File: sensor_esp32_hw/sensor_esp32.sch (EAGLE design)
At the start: 31 parts, among them IC1 ESP32-C3-WROOM-02-N4, IC2 ESP32-WROOM-32UE-N16, Q1 DMG3415, U1 AHT20, U2 TPL5110

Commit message: minor improvements before fabrication
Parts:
- added C10, C11: 100 nF, microbuilder:CAP_CERAMIC_0603
- C3: value 22 uF -> 10 uF
- PS1: value AP2202K-3.3TRG1 -> LDI8119-3.3EN-DIO
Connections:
- net GND: now also C10.2, C11.2
- net N$1: now also IC1.IO3; no longer IC1.IO2
- net PWROUT: now also C11.1; no longer C2.+
- net PWROUT_DIV: now also C10.1
- net VCC: now also C2.+
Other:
- moved on the sheet: C2, C3, PS1, R7

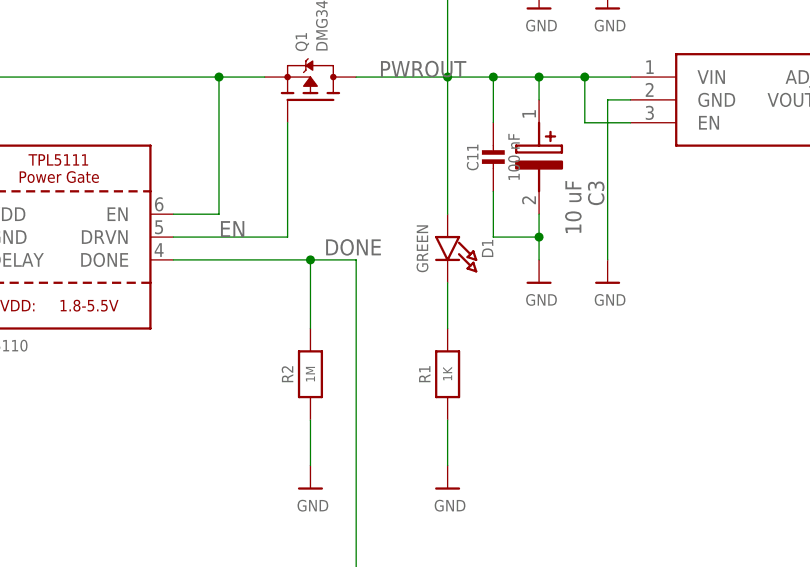
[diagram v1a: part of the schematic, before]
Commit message: fixes to schematic and pcb, also made esp32 sensor work
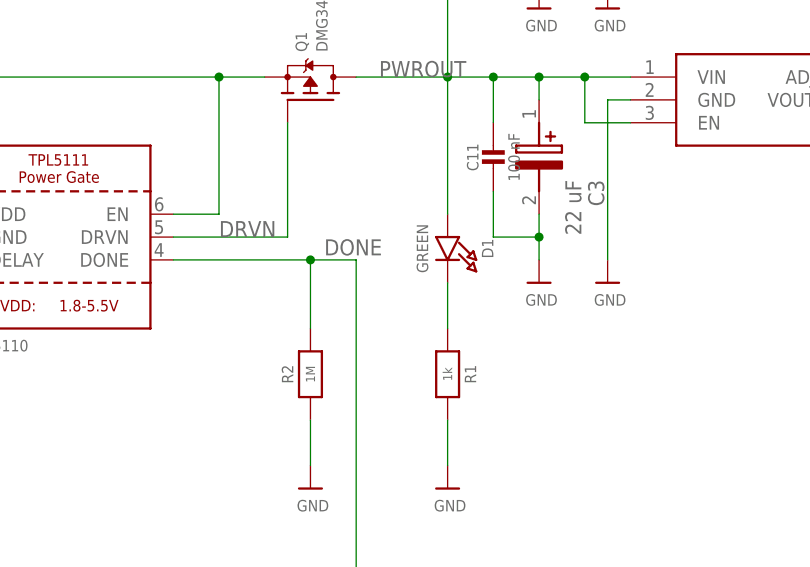
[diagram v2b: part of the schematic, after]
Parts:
- C3: value 10 uF -> 22 uF; DESCRIPTION (none) -> Solid Tantalum Surface Mount Chip Capacitors TANTAMOUNT(TM)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; HEIGHT (none) -> 1.8mm; MANUFACTURER_NAME (none) -> Vishay; MANUFACTURER_PART_NUMBER (none) -> 293D226X9010A2TE3
- C5: device microbuilder:CAP_CERAMIC0805-NOOUTLINE -> microbuilder:CAP_CERAMIC_0603
- R1: value 1K -> 1k; device microbuilder:RESISTOR0805_NOOUTLINE -> microbuilder:RESISTOR_0603
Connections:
- new net DRVN: Q1.G, U2.DRVN
- net EN: no longer Q1.G, U2.DRVN
- net GND: now also R1.2; no longer R1.1
- net N$3: now also R1.1; no longer R1.2
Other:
- moved on the sheet: R1
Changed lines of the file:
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@@
 <part name="Q1" library="microbuilder" deviceset="MOSFET-P" device="WIDE" value="DMG3415"/>
 <part name="D1" library="microbuilder" deviceset="LED" device="0805_NOOUTLINE" value="GREEN"/>
-<part name="R1" library="microbuilder" deviceset="RESISTOR" device="0805_NOOUTLINE" value="1K"/>
 <part name="U$6" library="microbuilder" deviceset="GND" device=""/>
 <part name="R2" library="microbuilder" deviceset="RESISTOR" device="_0603" value="1M"/>
@@
 <part name="JP1" library="jumper" deviceset="JP1E" device=""/>
 <part name="C2" library="293D107X9010C2TE3" deviceset="293D107X9010C2TE3" device="" value="100 uF"/>
-<part name="C3" library="293D226X9010A2TE3" deviceset="293D226X9010A2TE3" device="" value="10 uF"/>
 <part name="IC1" library="ESP32-C3-WROOM-02-N4" deviceset="ESP32-C3-WROOM-02-N4" device=""/>
 <part name="U$1" library="microbuilder" deviceset="GND" device=""/>
@@
 <part name="U$5" library="microbuilder" deviceset="GND" device=""/>
 <part name="U$8" library="microbuilder" deviceset="GND" device=""/>
-<part name="C5" library="microbuilder" deviceset="CAP_CERAMIC" device="0805-NOOUTLINE" value="100 nF"/>
 <part name="SV2" library="con-lstb" deviceset="MA03-1" device=""/>
 <part name="U$12" library="microbuilder" deviceset="GND" device=""/>
@@
 <part name="U$19" library="microbuilder" deviceset="GND" device=""/>
 <part name="C11" library="microbuilder" deviceset="CAP_CERAMIC" device="_0603" value="100 nF"/>
+<part name="C5" library="microbuilder" deviceset="CAP_CERAMIC" device="_0603" value="100 nF"/>
+<part name="R1" library="microbuilder" deviceset="RESISTOR" device="_0603" value="1k"/>
+<part name="C3" library="293D226X9010A2TE3" deviceset="293D226X9010A2TE3" device="" value="22 uF">
+<attribute name="DESCRIPTION" value="Solid Tantalum Surface Mount Chip Capacitors TANTAMOUNT(TM), Molded Case, Standard Industrial Grade"/>
+<attribute name="HEIGHT" value="1.8mm"/>
+<attribute name="MANUFACTURER_NAME" value="Vishay"/>
+<attribute name="MANUFACTURER_PART_NUMBER" value="293D226X9010A2TE3"/>
+<attribute name="TME_ELECTRONIC_COMPONENTS_PART_NUMBER" value=""/>
+<attribute name="TME_ELECTRONIC_COMPONENTS_PRICE-STOCK" value=""/>
+</part>
 </parts>
 <sheets>
@@
 <instance part="Q1" gate="G$1" x="160.02" y="109.22" rot="R90"/>
 <instance part="D1" gate="G$1" x="175.26" y="88.9" rot="R270"/>
-<instance part="R1" gate="G$1" x="175.26" y="76.2" rot="R90"/>
 <instance part="U$6" gate="G$1" x="175.26" y="63.5"/>
 <instance part="R2" gate="G$1" x="160.02" y="76.2" rot="R90"/>
@@
 <instance part="JP1" gate="A" x="83.82" y="96.52" rot="MR270"/>
 <instance part="C2" gate="G$1" x="228.6" y="104.14" rot="R270"/>
-<instance part="C3" gate="G$1" x="185.42" y="106.68" rot="R270"/>
 <instance part="IC1" gate="G$1" x="266.7" y="106.68"/>
 <instance part="U$1" gate="G$1" x="302.26" y="71.12"/>
@@
 <instance part="U$5" gate="G$1" x="193.04" y="86.36"/>
 <instance part="U$8" gate="G$1" x="236.22" y="83.82"/>
-<instance part="C5" gate="G$1" x="243.84" y="96.52"/>
 <instance part="SV2" gate="G$1" x="373.38" y="104.14" rot="R180"/>
 <instance part="U$12" gate="G$1" x="363.22" y="86.36"/>
@@
 <instance part="U$19" gate="G$1" x="193.04" y="116.84"/>
 <instance part="C11" gate="G$1" x="180.34" y="99.06"/>
+<instance part="C5" gate="G$1" x="243.84" y="96.52"/>
+<instance part="R1" gate="G$1" x="175.26" y="76.2" rot="R270"/>
+<instance part="C3" gate="G$1" x="185.42" y="106.68" rot="R270"/>
 </instances>
 <busses>
@@
 <net name="GND" class="0">
 <segment>
-<pinref part="R1" gate="G$1" pin="1"/>
 <wire x1="175.26" y1="71.12" x2="175.26" y2="66.04" width="0.1524" layer="91"/>
 <pinref part="U$6" gate="G$1" pin="GND"/>
+<pinref part="R1" gate="G$1" pin="2"/>
 </segment>
 <segment>
@@
 <segment>
 <pinref part="U$4" gate="G$1" pin="GND"/>
-<pinref part="C3" gate="G$1" pin="-"/>
 <wire x1="185.42" y1="88.9" x2="185.42" y2="91.44" width="0.1524" layer="91"/>
 <pinref part="C11" gate="G$1" pin="2"/>
@@
 <wire x1="180.34" y1="91.44" x2="185.42" y2="91.44" width="0.1524" layer="91"/>
 <junction x="185.42" y="91.44"/>
+<pinref part="C3" gate="G$1" pin="-"/>
 </segment>
 <segment>
@@
 <pinref part="C4" gate="G$1" pin="-"/>
 <wire x1="236.22" y1="91.44" x2="236.22" y2="88.9" width="0.1524" layer="91"/>
-<pinref part="C5" gate="G$1" pin="2"/>
 <wire x1="236.22" y1="88.9" x2="236.22" y2="86.36" width="0.1524" layer="91"/>
 <wire x1="243.84" y1="93.98" x2="243.84" y2="88.9" width="0.1524" layer="91"/>
@@
 <wire x1="228.6" y1="91.44" x2="228.6" y2="88.9" width="0.1524" layer="91"/>
 <wire x1="228.6" y1="88.9" x2="236.22" y2="88.9" width="0.1524" layer="91"/>
+<pinref part="C5" gate="G$1" pin="2"/>
 </segment>
 <segment>
@@
 <net name="EN" class="0">
 <segment>
-<pinref part="U2" gate="G$1" pin="DRVN"/>
-<wire x1="144.78" y1="91.44" x2="157.48" y2="91.44" width="0.1524" layer="91"/>
-<label x="149.86" y="91.44" size="1.778" layer="95"/>
-<pinref part="Q1" gate="G$1" pin="G"/>
-<wire x1="157.48" y1="104.14" x2="157.48" y2="91.44" width="0.1524" layer="91"/>
-</segment>
-<segment>
 <pinref part="SV1" gate="G$1" pin="2"/>
 <label x="266.954" y="145.034" size="0.8128" layer="95"/>
@@
 <wire x1="175.26" y1="109.22" x2="175.26" y2="93.98" width="0.1524" layer="91"/>
 <wire x1="175.26" y1="109.22" x2="180.34" y2="109.22" width="0.1524" layer="91"/>
-<pinref part="C3" gate="G$1" pin="+"/>
 <wire x1="180.34" y1="109.22" x2="185.42" y2="109.22" width="0.1524" layer="91"/>
 <wire x1="185.42" y1="109.22" x2="185.42" y2="106.68" width="0.1524" layer="91"/>
@@
 <wire x1="180.34" y1="104.14" x2="180.34" y2="109.22" width="0.1524" layer="91"/>
 <junction x="180.34" y="109.22"/>
+<pinref part="C3" gate="G$1" pin="+"/>
 </segment>
 </net>
 <net name="N$3" class="0">
 <segment>
-<pinref part="R1" gate="G$1" pin="2"/>
 <pinref part="D1" gate="G$1" pin="C"/>
 <wire x1="175.26" y1="81.28" x2="175.26" y2="86.36" width="0.1524" layer="91"/>
+<pinref part="R1" gate="G$1" pin="1"/>
 </segment>
 </net>
@@
 <pinref part="IC1" gate="G$1" pin="3V3"/>
 <label x="256.54" y="106.934" size="0.8128" layer="95"/>
-<pinref part="C5" gate="G$1" pin="1"/>
 <wire x1="243.84" y1="106.68" x2="249.936" y2="106.68" width="0.1524" layer="91"/>
 <wire x1="249.936" y1="106.68" x2="266.7" y2="106.68" width="0.1524" layer="91"/>
@@
 <wire x1="228.6" y1="104.14" x2="228.6" y2="106.68" width="0.1524" layer="91"/>
 <junction x="228.6" y="106.68"/>
+<pinref part="C5" gate="G$1" pin="1"/>
 </segment>
 <segment>
@@
 </segment>
 </net>
+<net name="DRVN" class="0">
+<segment>
+<pinref part="U2" gate="G$1" pin="DRVN"/>
+<wire x1="144.78" y1="91.44" x2="157.48" y2="91.44" width="0.1524" layer="91"/>
+<label x="149.86" y="91.44" size="1.778" layer="95"/>
+<pinref part="Q1" gate="G$1" pin="G"/>
+<wire x1="157.48" y1="104.14" x2="157.48" y2="91.44" width="0.1524" layer="91"/>
+</segment>
+</net>

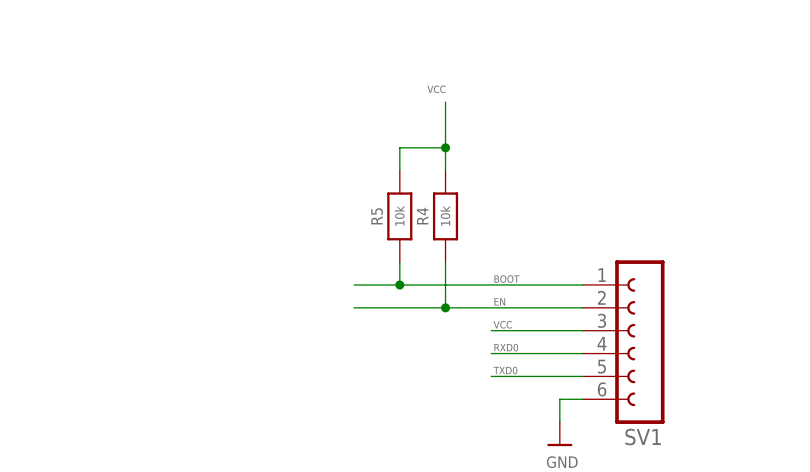
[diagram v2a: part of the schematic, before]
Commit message: added pull up on BOOT1 for flashing via serial
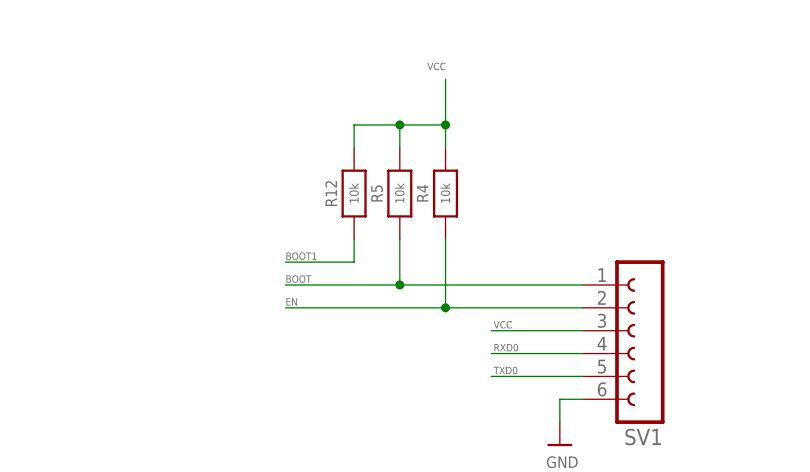
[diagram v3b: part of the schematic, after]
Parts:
- added R12: 10k, microbuilder:RESISTOR_0603
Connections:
- net BOOT1: now also R12.1
- net VCC: now also R12.2
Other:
- moved on the sheet: R4, R5
